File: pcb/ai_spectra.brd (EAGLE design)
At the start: 127 x 127 mm, 97 parts, among them IC1 ATMEGA328P-PDIP, J1 1X06, J3 1X02ST, U1 MC7805-HOR, U2 TLC2262

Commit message: adding gerbers
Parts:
- removed J1: 1X06, Ai_Connectors:1X06
- removed PR1, PR2: LDR-PTH, Ai_Sensors:LDR
- removed S1: SW-SPSTTH06X06, Ai_Electromechanical:SW-SPST-TH06X06
- removed VR1: 10K, Ai_Passives:POT-05X05
- added FTDI: 1X06, Ai_Connectors:1X06
- added LDR1, LDR2: LDR-PTH, Ai_Sensors:LDR
- added RESET: SW-SPSTTH06X06, Ai_Electromechanical:SW-SPST-TH06X06
- added U$18: AI-LOGOXS, Ai_Miscellany:AI-LOGO-XS
- added VOLUME: 10K, Ai_Passives:POT-05X05
- LED1, LED10, LED11, LED12, LED13, LED14, LED15, LED16, LED17, LED18, LED19, LED2, LED20, LED21, LED22, LED23, LED24, LED25, LED26, LED27, LED28, LED29, LED3, LED30, LED31, LED32, LED33, LED34, LED35, LED36, LED37, LED38, LED39, LED4, LED40, LED41, LED42, LED43, LED44, LED45, LED46, LED47, LED48, LED5, LED6, LED7, LED8, LED9: value LED-PL9823-F5 -> LED-PL9823-F8; device Ai_LED:LED-PL9823-F5 -> Ai_LED:LED-PL9823-F8
- moved STANDOFF3 18.0 mm to (137.2, 137.2)
- moved LED7 14.1 mm to (116.1, 116.1)
- moved LED6 14.0 mm to (109.7, 121.7)
- moved LED8 14.0 mm to (121.7, 109.7)
- moved LED5 13.9 mm to (102.6, 126.5)
- moved LED9 13.9 mm to (126.5, 102.6)
- moved LED10 13.8 mm to (130.3, 94.9)
- moved LED4 13.8 mm to (94.9, 130.3)
- moved LED11 13.6 mm to (133.0, 86.8)
- moved LED3 13.6 mm to (86.8, 133.0)
- moved LED12 13.4 mm to (134.7, 78.4)
- moved LED2 13.4 mm to (78.4, 134.7)
- moved LED1 13.1 mm to (69.8, 135.3)
- moved LED13 13.1 mm to (135.3, 69.8)
- moved LED14 12.7 mm to (134.7, 61.3)
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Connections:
- net 5V: now also FTDI.3; no longer J1.3
- net GND: now also FTDI.1, LDR1.1, LDR2.1, RESET.A@1, VOLUME.3; no longer J1.1, PR1.1, PR2.1, S1.A@1, VR1.3
- net LDR1: now also LDR2.2; no longer PR1.2
- net LDR2: now also LDR1.2; no longer PR2.2
- net N$1: now also VOLUME.2; no longer VR1.2
- net RESET: now also FTDI.6, RESET.B@1; no longer J1.6, S1.B@1
- net RXI: now also FTDI.4; no longer J1.4
- net SND_CLN: now also VOLUME.1; no longer VR1.1
- net TXO: now also FTDI.5; no longer J1.5
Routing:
- net 5V: track 571.5 -> 676.1 mm
- net VDD: track 159.6 -> 176.9 mm
- net RXI: track 47.9 -> 59.1 mm
- net TXO: track 51.2 -> 61.3 mm
- net RESET: track 96.9 -> 106.0 mm
- net D: track 8.84 -> 14.7 mm
- net ENC2_B: track 104.0 -> 109.4 mm
- net VIN: track 32.6 -> 35.5 mm
- net N$13: track 55.7 -> 53.2 mm
- net ENC1_A: track 91.1 -> 89.0 mm
- net N$12: track 30.1 -> 31.9 mm
- net N$5: track 21.4 -> 19.9 mm
- net LDR2: track 86.2 -> 87.4 mm
- net N$42: track 4.07 -> 4.75 mm
- net N$38: track 4.07 -> 4.75 mm
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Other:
- board size 127 x 127 mm -> 139.7 x 139.7 mm
- board text added: "5V"
- board text added: "ACROBOTIC Spectra"
- board text added: "DTR"
- board text added: "Design by: Sonia Parada"
- board text added: "GND"
- board text added: "IN"
- board text added: "OUT"
- board text added: "RXD"
- board text added: "TXD"
- board text added: "http://acrobotic.com/spectra"
- board text added: "v1.0"

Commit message: updating license, and schematic
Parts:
- added FRAME1, FRAME2: FRAME-LETTER, Ai_Miscellany:CREATIVE-COMMONS
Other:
- board text added: "Sonia P."
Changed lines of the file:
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@@
 <setting verticaltext="up"/>
 </settings>
-<grid distance="25" unitdist="mil" unit="mil" style="lines" multiple="1" display="yes" altdistance="0.025" altunitdist="inch" altunit="inch"/>
+<grid distance="50" unitdist="mil" unit="mil" style="lines" multiple="1" display="yes" altdistance="0.025" altunitdist="inch" altunit="inch"/>
 <layers>
 <layer number="1" name="Top" color="4" fill="1" visible="yes" active="yes"/>
@@
 <layer number="20" name="Dimension" color="15" fill="1" visible="yes" active="yes"/>
 <layer number="21" name="tPlace" color="7" fill="1" visible="yes" active="yes"/>
-<layer number="22" name="bPlace" color="7" fill="1" visible="yes" active="yes"/>
+<layer number="22" name="bPlace" color="13" fill="1" visible="yes" active="yes"/>
 <layer number="23" name="tOrigins" color="15" fill="1" visible="yes" active="yes"/>
 <layer number="24" name="bOrigins" color="15" fill="1" visible="yes" active="yes"/>
@@
 <layer number="49" name="Reference" color="7" fill="1" visible="yes" active="yes"/>
 <layer number="50" name="dxf" color="7" fill="1" visible="no" active="no"/>
-<layer number="51" name="tDocu" color="7" fill="1" visible="no" active="yes"/>
-<layer number="52" name="bDocu" color="7" fill="1" visible="no" active="yes"/>
+<layer number="51" name="tDocu" color="14" fill="1" visible="yes" active="yes"/>
+<layer number="52" name="bDocu" color="7" fill="1" visible="yes" active="yes"/>
 <layer number="53" name="tGND_GNDA" color="7" fill="9" visible="no" active="no"/>
 <layer number="54" name="bGND_GNDA" color="1" fill="9" visible="no" active="no"/>
@@
 <circle x="84.455" y="54.61" radius="1.5875" width="0.0254" layer="20"/>
 <circle x="84.455" y="44.45" radius="1.5875" width="0.0254" layer="20"/>
+<text x="69.85" y="-16.51" size="1.524" layer="51" font="vector" ratio="10" align="center">Sonia P.</text>
 </plain>
 <attributes>
@@
 </element>
 <element name="U$18" library="Ai_Miscellany" package="AI-LOGO-XS" value="AI-LOGOXS" x="131.318" y="136.779"/>
+<element name="FRAME1" library="Ai_Miscellany" package="CREATIVE-COMMONS" value="FRAME-LETTER" x="69.85" y="-1.27">
+<attribute name="REV" value="1.0" x="69.85" y="-1.27" size="1.778" layer="27" display="off"/>
+</element>
+<element name="FRAME2" library="Ai_Miscellany" package="CREATIVE-COMMONS" value="FRAME-LETTER" x="69.85" y="-1.27">
+<attribute name="REV" value="1.0" x="69.85" y="-1.27" size="1.778" layer="27" display="off"/>
+</element>
 </elements>
 <signals>
@@
 </board>
 </drawing>
+<compatibility>
+<note version="6.3" minversion="6.2.2" severity="warning">
+Since Version 6.2.2 text objects can contain more than one line,
+which will not be processed correctly with this version.
+</note>
+</compatibility>
 </eagle>

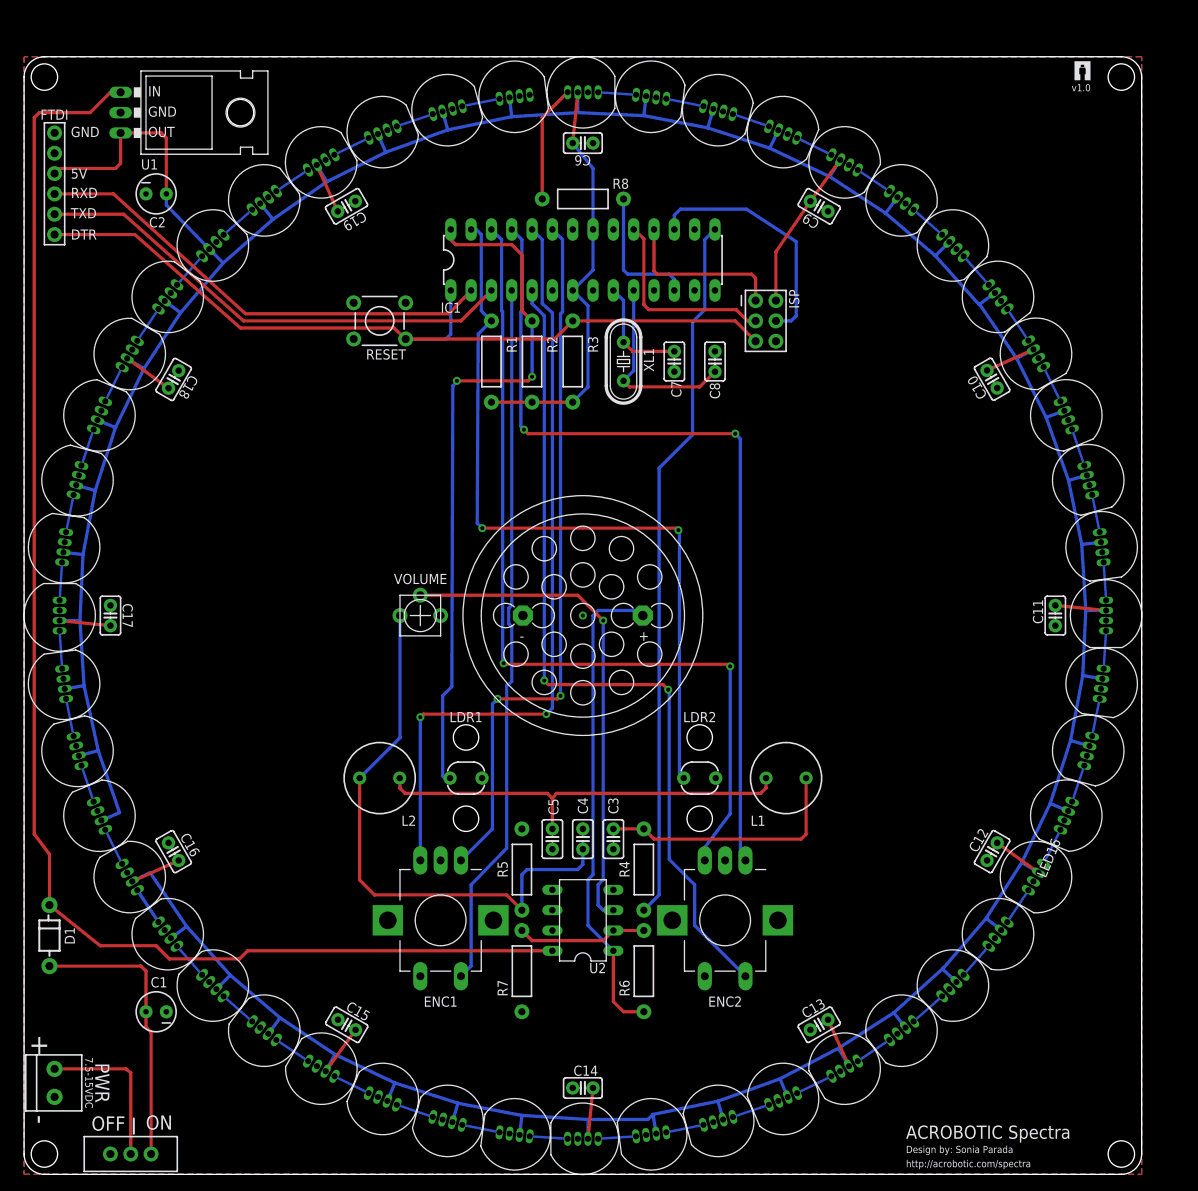
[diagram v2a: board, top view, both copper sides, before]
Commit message: updating LED spacing
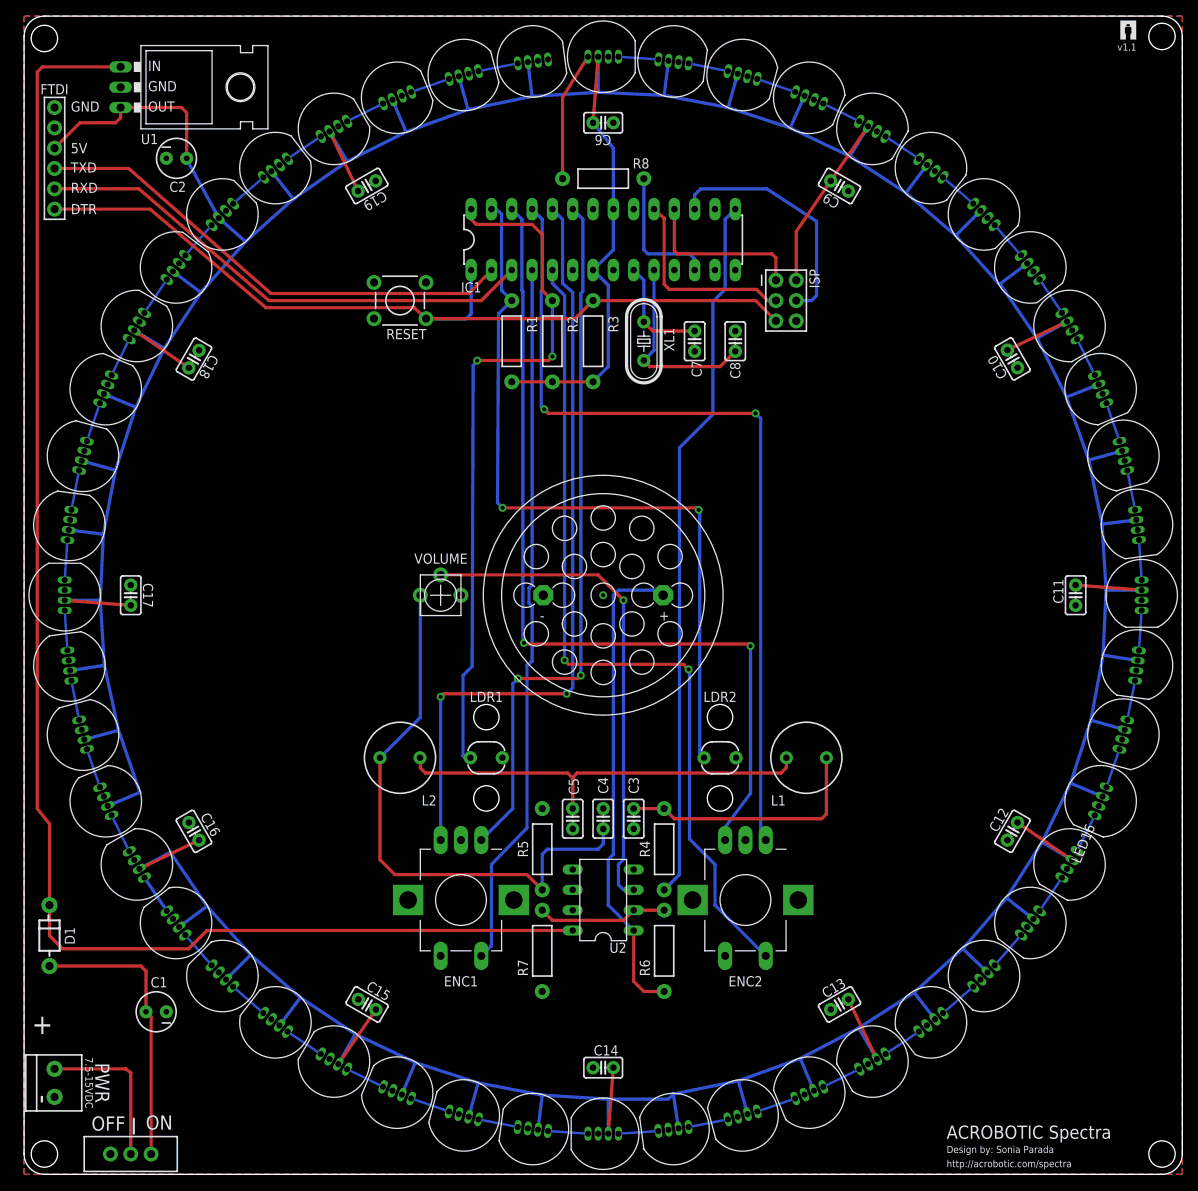
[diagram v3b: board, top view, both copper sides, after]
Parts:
- moved U$18 7.65 mm to (137.0, 141.9)
- moved STANDOFF3 7.18 mm to (142.2, 142.2)
- moved LED7 5.50 mm to (120.0, 120.0)
- moved LED6 5.47 mm to (113.4, 125.8)
- moved LED8 5.47 mm to (125.8, 113.4)
- moved LED5 5.45 mm to (106.0, 130.7)
- moved LED9 5.45 mm to (130.7, 106.0)
- moved LED10 5.40 mm to (134.6, 98.1)
- moved LED4 5.40 mm to (98.1, 134.6)
- moved LED11 5.35 mm to (137.4, 89.8)
- moved LED3 5.35 mm to (89.8, 137.4)
- moved LED12 5.23 mm to (139.1, 81.2)
- moved LED2 5.23 mm to (81.2, 139.1)
- moved LED1 5.12 mm to (72.4, 139.7)
- moved LED13 5.12 mm to (139.7, 72.4)
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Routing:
- net 5V: track 676.1 -> 789.5 mm
- net VDD: track 176.9 -> 186.2 mm
- net RESET: track 106.0 -> 108.6 mm
- net TXO: track 61.3 -> 63.9 mm
- net RXI: track 59.1 -> 61.7 mm
- net D: track 14.7 -> 16.2 mm
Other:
- board size 139.7 x 139.7 mm -> 144.8 x 144.8 mm
- board text added: "v1.1"
- board text removed: "v1.0"
